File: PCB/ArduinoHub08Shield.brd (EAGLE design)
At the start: 57.1 x 53.3 mm, 2 parts

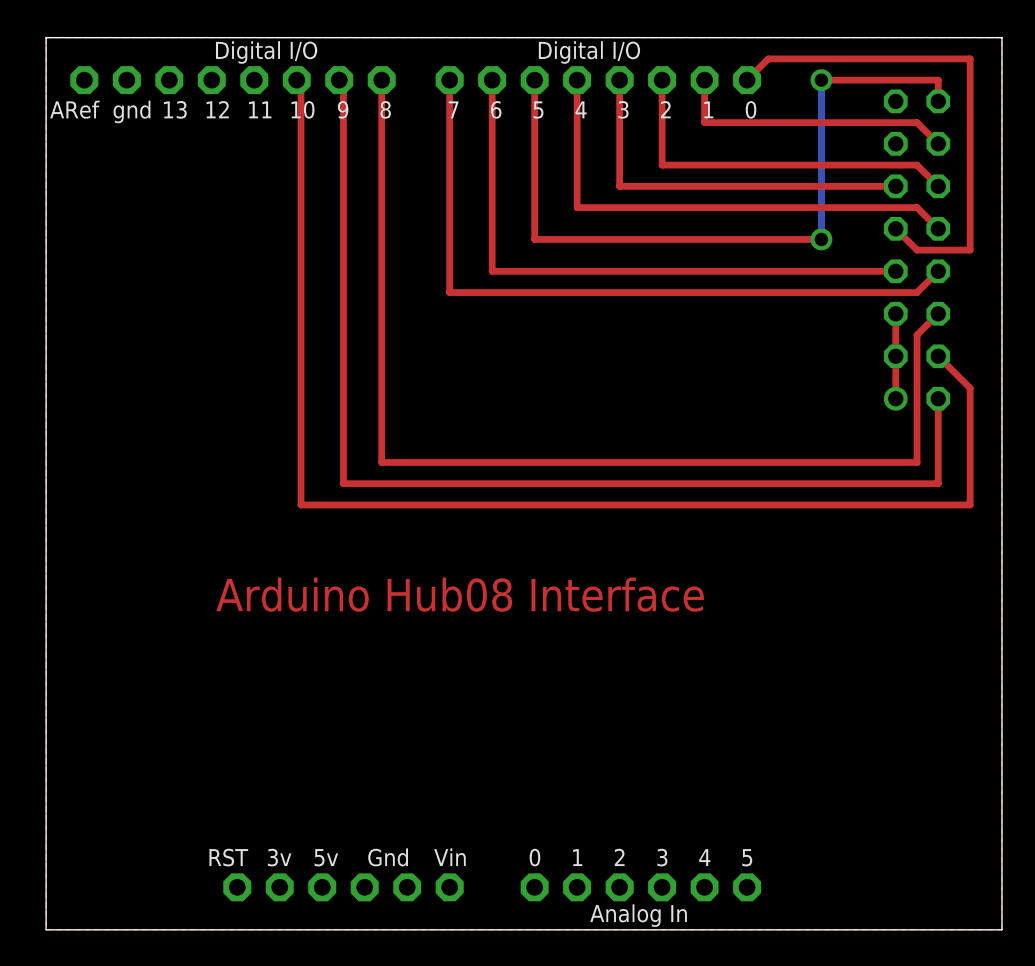
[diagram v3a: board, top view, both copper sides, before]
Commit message: Hardware Update (Schematic/PCB and Hardware.h)
Because we cant use the digital pins 0,1 on Yun, we updated
the schematic and layout to use different pins.

Now the A-D address lines are also on the high nibble of
PORTB, which leave some room for even more tuning of the
ISR.
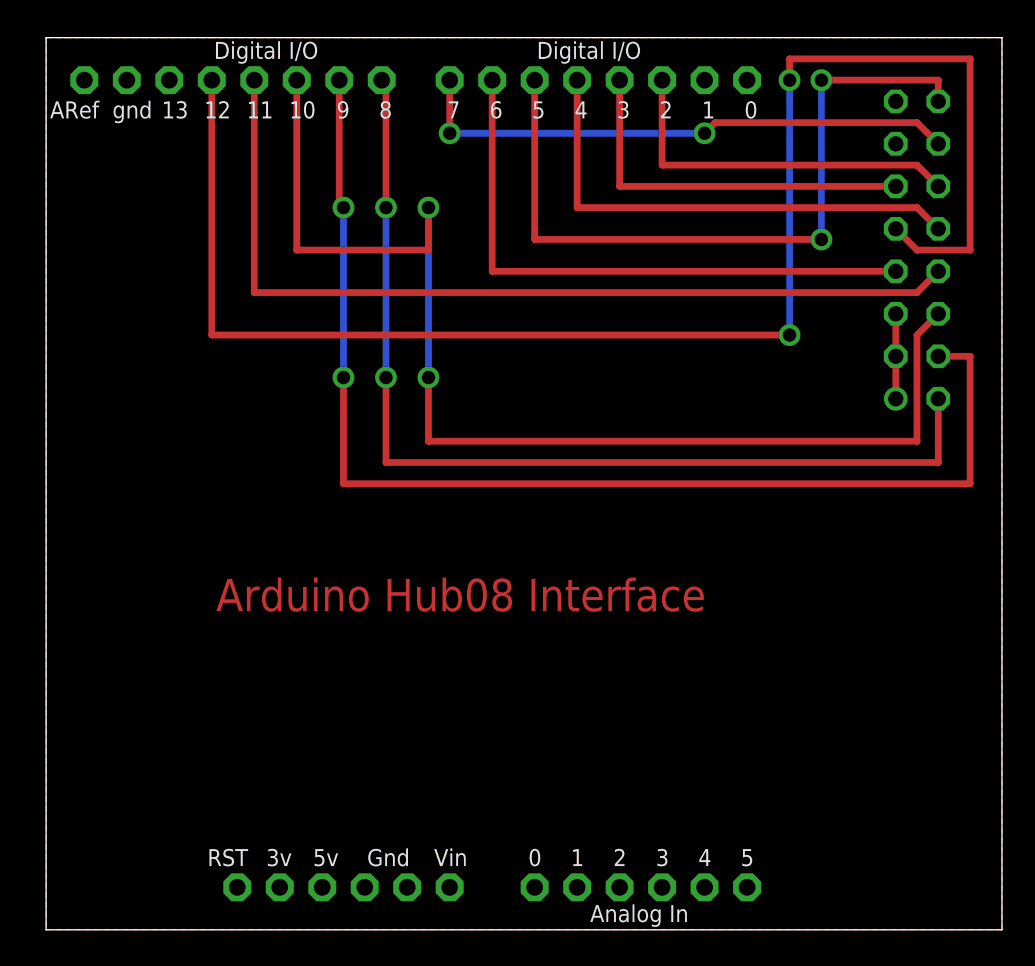
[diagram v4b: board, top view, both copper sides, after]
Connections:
- net A: now also U$1.D8; no longer U$1.D9
- net B: now also U$1.D9; no longer U$1.D10
- net C: now also U$1.D10; no longer U$1.D8
- net D: now also U$1.D11; no longer U$1.D7
- net L: now also U$1.D7; no longer U$1.D1
- net R1: now also U$1.D12; no longer U$1.D0
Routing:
- net R1: track 30.3 -> 93.5 mm, vias 0 -> 2
- net L: track 17.0 -> 33.2 mm, vias 0 -> 2
- net D: track 42.4 -> 54.1 mm
- net C: track 64.3 -> 71.9 mm, vias 0 -> 2
- net A: track 65.0 -> 59.9 mm, vias 0 -> 2
- net B: track 75.3 -> 71.4 mm, vias 0 -> 2
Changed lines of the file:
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@@
 <signal name="R1">
 <contactref element="CON1" pad="9"/>
-<contactref element="U$1" pad="D0"/>
 <wire x1="72.39" y1="41.91" x2="73.66" y2="40.64" width="0.4064" layer="1"/>
 <wire x1="73.66" y1="40.64" x2="76.835" y2="40.64" width="0.4064" layer="1"/>
 <wire x1="76.835" y1="40.64" x2="76.835" y2="52.07" width="0.4064" layer="1"/>
-<wire x1="76.835" y1="52.07" x2="64.77" y2="52.07" width="0.4064" layer="1"/>
-<wire x1="64.77" y1="52.07" x2="63.5" y2="50.8" width="0.4064" layer="1"/>
+<wire x1="76.835" y1="52.07" x2="66.04" y2="52.07" width="0.4064" layer="1"/>
+<contactref element="U$1" pad="D12"/>
+<wire x1="66.04" y1="52.07" x2="66.04" y2="50.8" width="0.4064" layer="1"/>
+<via x="66.04" y="50.8" extent="1-16" drill="0.8" shape="square"/>
+<wire x1="66.04" y1="50.8" x2="66.04" y2="35.56" width="0.4064" layer="16"/>
+<via x="66.04" y="35.56" extent="1-16" drill="0.8" shape="square"/>
+<wire x1="66.04" y1="35.56" x2="31.496" y2="35.56" width="0.4064" layer="1"/>
+<wire x1="31.496" y1="35.56" x2="31.496" y2="50.8" width="0.4064" layer="1"/>
 </signal>
 <signal name="L">
 <contactref element="CON1" pad="14"/>
-<contactref element="U$1" pad="D1"/>
 <wire x1="74.93" y1="46.99" x2="73.66" y2="48.26" width="0.4064" layer="1"/>
-<wire x1="73.66" y1="48.26" x2="60.96" y2="48.26" width="0.4064" layer="1"/>
-<wire x1="60.96" y1="48.26" x2="60.96" y2="50.8" width="0.4064" layer="1"/>
+<contactref element="U$1" pad="D7"/>
+<via x="60.96" y="47.625" extent="1-16" drill="0.8" shape="square"/>
+<wire x1="60.96" y1="47.625" x2="45.72" y2="47.625" width="0.4064" layer="16"/>
+<via x="45.72" y="47.625" extent="1-16" drill="0.8" shape="square"/>
+<wire x1="45.72" y1="47.625" x2="45.72" y2="50.8" width="0.4064" layer="1"/>
+<wire x1="73.66" y1="48.26" x2="61.595" y2="48.26" width="0.4064" layer="1"/>
+<wire x1="61.595" y1="48.26" x2="60.96" y2="47.625" width="0.4064" layer="1"/>
 </signal>
 <signal name="S">
@@
 <signal name="D">
 <contactref element="CON1" pad="8"/>
-<contactref element="U$1" pad="D7"/>
 <wire x1="74.93" y1="39.37" x2="73.66" y2="38.1" width="0.4064" layer="1"/>
-<wire x1="73.66" y1="38.1" x2="45.72" y2="38.1" width="0.4064" layer="1"/>
-<wire x1="45.72" y1="38.1" x2="45.72" y2="50.8" width="0.4064" layer="1"/>
+<wire x1="73.66" y1="38.1" x2="34.036" y2="38.1" width="0.4064" layer="1"/>
+<contactref element="U$1" pad="D11"/>
+<wire x1="34.036" y1="38.1" x2="34.036" y2="50.8" width="0.4064" layer="1"/>
 </signal>
 <signal name="C">
 <contactref element="CON1" pad="6"/>
-<contactref element="U$1" pad="D8"/>
 <wire x1="74.93" y1="36.83" x2="73.66" y2="35.56" width="0.4064" layer="1"/>
-<wire x1="73.66" y1="35.56" x2="73.66" y2="27.94" width="0.4064" layer="1"/>
-<wire x1="73.66" y1="27.94" x2="41.656" y2="27.94" width="0.4064" layer="1"/>
-<wire x1="41.656" y1="27.94" x2="41.656" y2="50.8" width="0.4064" layer="1"/>
+<wire x1="73.66" y1="35.56" x2="73.66" y2="29.21" width="0.4064" layer="1"/>
+<contactref element="U$1" pad="D10"/>
+<via x="44.45" y="33.02" extent="1-16" drill="0.8" shape="square"/>
+<wire x1="44.45" y1="33.02" x2="44.45" y2="43.18" width="0.4064" layer="16"/>
+<via x="44.45" y="43.18" extent="1-16" drill="0.8" shape="square"/>
+<wire x1="36.576" y1="40.64" x2="36.576" y2="50.8" width="0.4064" layer="1"/>
+<wire x1="36.576" y1="40.64" x2="44.45" y2="40.64" width="0.4064" layer="1"/>
+<wire x1="44.45" y1="40.64" x2="44.45" y2="43.18" width="0.4064" layer="1"/>
+<wire x1="73.66" y1="29.21" x2="44.45" y2="29.21" width="0.4064" layer="1"/>
+<wire x1="44.45" y1="29.21" x2="44.45" y2="33.02" width="0.4064" layer="1"/>
 </signal>
 <signal name="B">
 <contactref element="CON1" pad="4"/>
-<wire x1="74.93" y1="34.29" x2="76.835" y2="32.385" width="0.4064" layer="1"/>
-<wire x1="76.835" y1="32.385" x2="76.835" y2="25.4" width="0.4064" layer="1"/>
-<wire x1="76.835" y1="25.4" x2="36.83" y2="25.4" width="0.4064" layer="1"/>
-<contactref element="U$1" pad="D10"/>
-<wire x1="36.576" y1="50.8" x2="36.83" y2="50.8" width="0.4064" layer="1"/>
-<wire x1="36.83" y1="50.8" x2="36.83" y2="25.4" width="0.4064" layer="1"/>
+<contactref element="U$1" pad="D9"/>
+<wire x1="74.93" y1="34.29" x2="76.835" y2="34.29" width="0.4064" layer="1"/>
+<wire x1="76.835" y1="34.29" x2="76.835" y2="26.67" width="0.4064" layer="1"/>
+<wire x1="76.835" y1="26.67" x2="39.37" y2="26.67" width="0.4064" layer="1"/>
+<wire x1="39.37" y1="26.67" x2="39.37" y2="33.02" width="0.4064" layer="1"/>
+<via x="39.37" y="33.02" extent="1-16" drill="0.8" shape="square"/>
+<wire x1="39.37" y1="33.02" x2="39.37" y2="43.18" width="0.4064" layer="16"/>
+<via x="39.37" y="43.18" extent="1-16" drill="0.8" shape="square"/>
+<wire x1="39.37" y1="43.18" x2="39.116" y2="43.18" width="0.4064" layer="1"/>
+<wire x1="39.116" y1="43.18" x2="39.116" y2="50.8" width="0.4064" layer="1"/>
 </signal>
 <signal name="A">
 <contactref element="CON1" pad="2"/>
-<wire x1="74.93" y1="31.75" x2="74.93" y2="26.67" width="0.4064" layer="1"/>
-<wire x1="74.93" y1="26.67" x2="39.37" y2="26.67" width="0.4064" layer="1"/>
-<contactref element="U$1" pad="D9"/>
-<wire x1="39.116" y1="50.8" x2="39.37" y2="50.8" width="0.4064" layer="1"/>
-<wire x1="39.37" y1="50.8" x2="39.37" y2="26.67" width="0.4064" layer="1"/>
+<contactref element="U$1" pad="D8"/>
+<wire x1="74.93" y1="31.75" x2="74.93" y2="27.94" width="0.4064" layer="1"/>
+<wire x1="74.93" y1="27.94" x2="41.91" y2="27.94" width="0.4064" layer="1"/>
+<wire x1="41.91" y1="27.94" x2="41.91" y2="33.02" width="0.4064" layer="1"/>
+<via x="41.91" y="33.02" extent="1-16" drill="0.8" shape="square"/>
+<wire x1="41.91" y1="33.02" x2="41.91" y2="43.18" width="0.4064" layer="16"/>
+<via x="41.91" y="43.18" extent="1-16" drill="0.8" shape="square"/>
+<wire x1="41.656" y1="50.8" x2="41.91" y2="50.8" width="0.4064" layer="1"/>
+<wire x1="41.91" y1="50.8" x2="41.91" y2="43.18" width="0.4064" layer="1"/>
 </signal>
 <signal name="EN">

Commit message: PCB/schematic update: LDR light sensor added
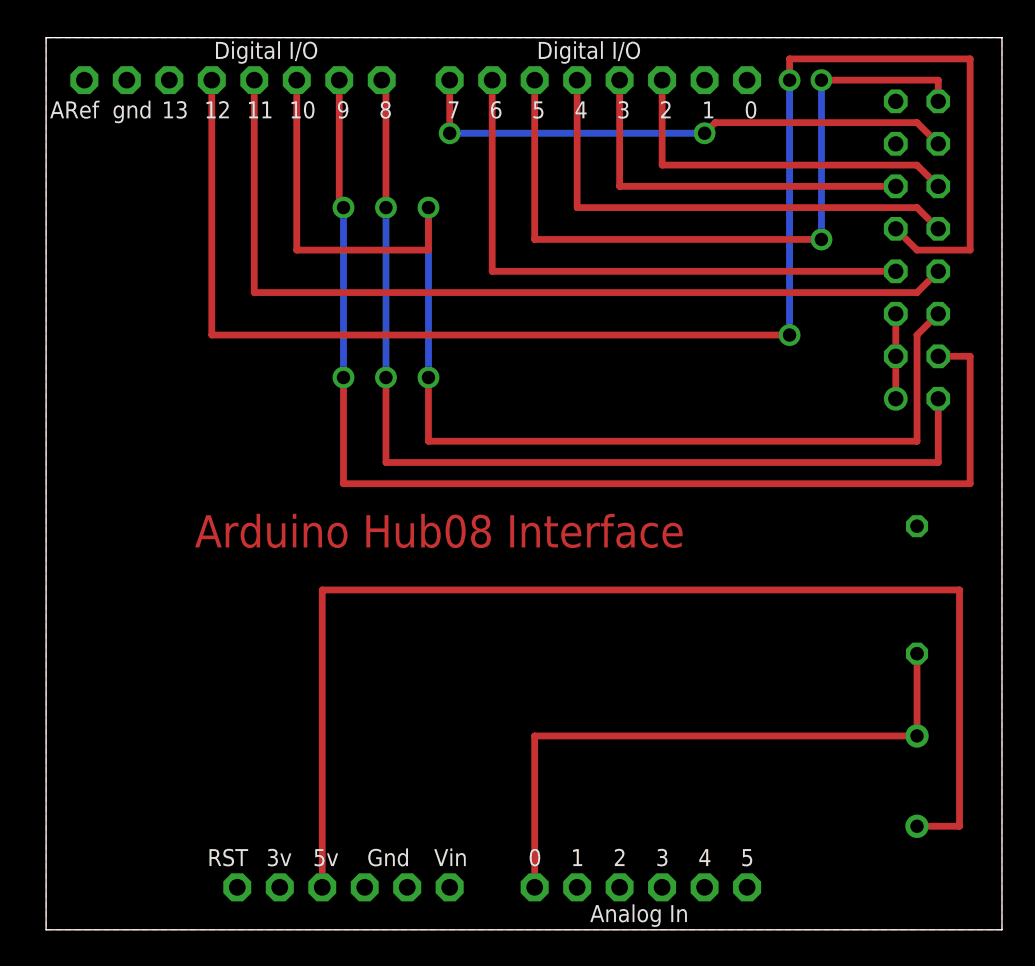
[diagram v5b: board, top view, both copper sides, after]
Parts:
- added PH1: V1060_21, photo-elements:TO-5_V10
- added R1: 10K, rcl:0204/7
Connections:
- removed net 5V: U$1.5V
- new net N$1: PH1.2, R1.2, U$1.A0
- new net VCC: PH1.1, U$1.5V
- net GND: now also CON1.13, CON1.15, R1.1
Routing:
- net VCC: track 0.00 -> 72.6 mm
- net N$1: track 0.00 -> 36.8 mm
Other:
- board text removed: ">LAST_DATE_TIME"
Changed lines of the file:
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@@
 <wire x1="78.74" y1="53.34" x2="78.74" y2="0" width="0" layer="20"/>
 <wire x1="78.74" y1="0" x2="21.59" y2="0" width="0" layer="20"/>
-<text x="31.75" y="19.05" size="1.9304" layer="1" font="vector" ratio="15">Arduino Hub08 Interface</text>
-<text x="31.75" y="16.51" size="1.9304" layer="1" font="vector" ratio="15" rot="R180" align="bottom-right">&gt;LAST_DATE_TIME</text>
+<text x="30.48" y="22.86" size="1.9304" layer="1" font="vector" ratio="15">Arduino Hub08 Interface</text>
 </plain>
 <attributes>
@@
 <param name="mdWireWire" value="12mil"/>
 <param name="mdWirePad" value="12mil"/>
-<param name="mdWireVia" value="8mil"/>
+<param name="mdWireVia" value="16mil"/>
 <param name="mdPadPad" value="8mil"/>
 <param name="mdPadVia" value="8mil"/>
@@
 </element>
 <element name="U$1" library="adafruit" package="ARDUINO-NOHOLE" value="ARDUINO-NOHOLE" x="0" y="0" smashed="yes"/>
+<element name="R1" library="rcl" package="0204/7" value="10K" x="73.66" y="20.32" rot="MR270"/>
+<element name="PH1" library="photo-elements" package="TO-5_V10" value="V1060_21" x="73.66" y="8.89" rot="MR90"/>
 </elements>
 <signals>
@@
 <signal name="GND2">
 <contactref element="U$1" pad="GND2"/>
-</signal>
-<signal name="5V">
-<contactref element="U$1" pad="5V"/>
 </signal>
 <signal name="3V">
@@
 <wire x1="72.39" y1="31.75" x2="72.39" y2="34.29" width="0.4064" layer="1"/>
 <wire x1="72.39" y1="34.29" x2="72.39" y2="36.83" width="0.4064" layer="1"/>
+<contactref element="R1" pad="1"/>
+<contactref element="CON1" pad="13"/>
+<contactref element="CON1" pad="15"/>
 </signal>
 <signal name="R1">
@@
 <wire x1="58.42" y1="45.72" x2="58.42" y2="50.8" width="0.4064" layer="1"/>
 </signal>
+<signal name="N$1">
+<contactref element="U$1" pad="A0"/>
+<contactref element="R1" pad="2"/>
+<contactref element="PH1" pad="2"/>
+<wire x1="50.8" y1="2.54" x2="50.8" y2="11.59" width="0.4064" layer="1"/>
+<wire x1="50.8" y1="11.59" x2="73.66" y2="11.59" width="0.4064" layer="1"/>
+<wire x1="73.66" y1="11.59" x2="73.66" y2="16.51" width="0.4064" layer="1"/>
+</signal>
+<signal name="VCC">
+<contactref element="U$1" pad="5V"/>
+<contactref element="PH1" pad="1"/>
+<wire x1="73.66" y1="6.19" x2="76.2" y2="6.19" width="0.4064" layer="1"/>
+<wire x1="76.2" y1="6.19" x2="76.2" y2="20.32" width="0.4064" layer="1"/>
+<wire x1="76.2" y1="20.32" x2="38.1" y2="20.32" width="0.4064" layer="1"/>
+<wire x1="38.1" y1="20.32" x2="38.1" y2="2.54" width="0.4064" layer="1"/>
+</signal>
 </signals>
